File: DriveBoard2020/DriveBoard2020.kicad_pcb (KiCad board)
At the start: 2 copper layers, 124.5 x 107.4 mm, 69 parts, among them SW0 SW_SPST, SW1 SW_Push, SW3 SW_Push, SW5 SW_Push, SW7 SW_Push, SW8 SW_Push, SW9 SW_Push, U1 MAX_3232, U2 MAX_3232, U3 OKI, U4 TM4C129E_Launchpad, U5 MAX_3232, U6 OKI, U7 OKI, U8 LDD-1500L

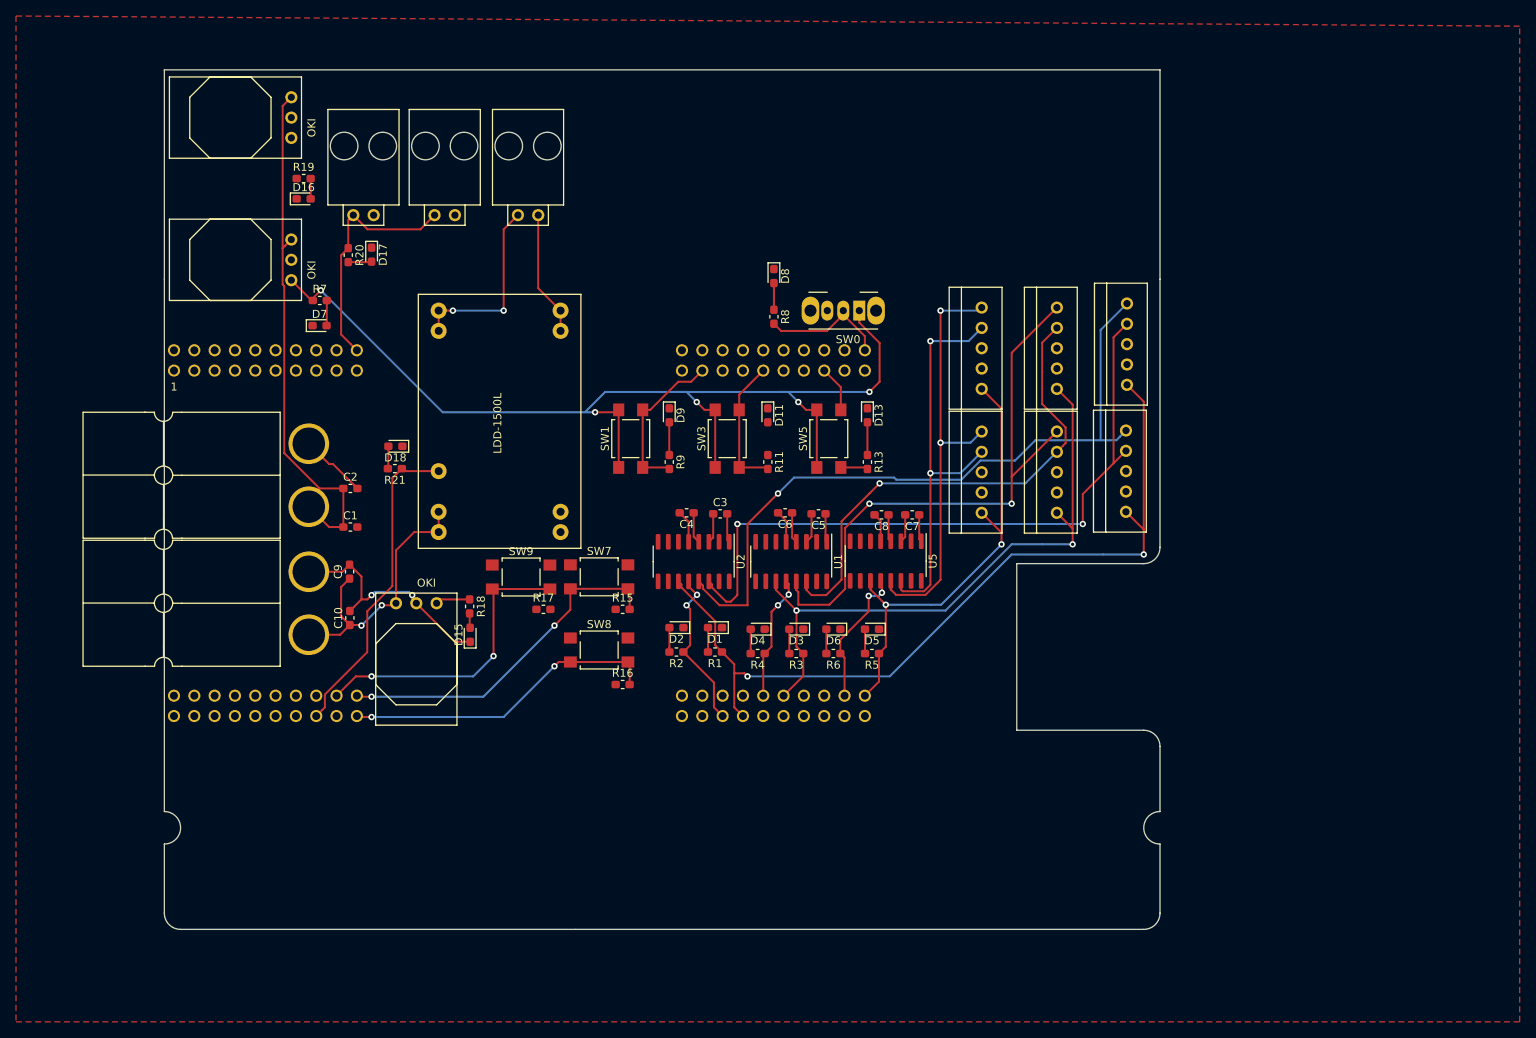
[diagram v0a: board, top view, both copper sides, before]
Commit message: cleaned up layout and generated gerbs
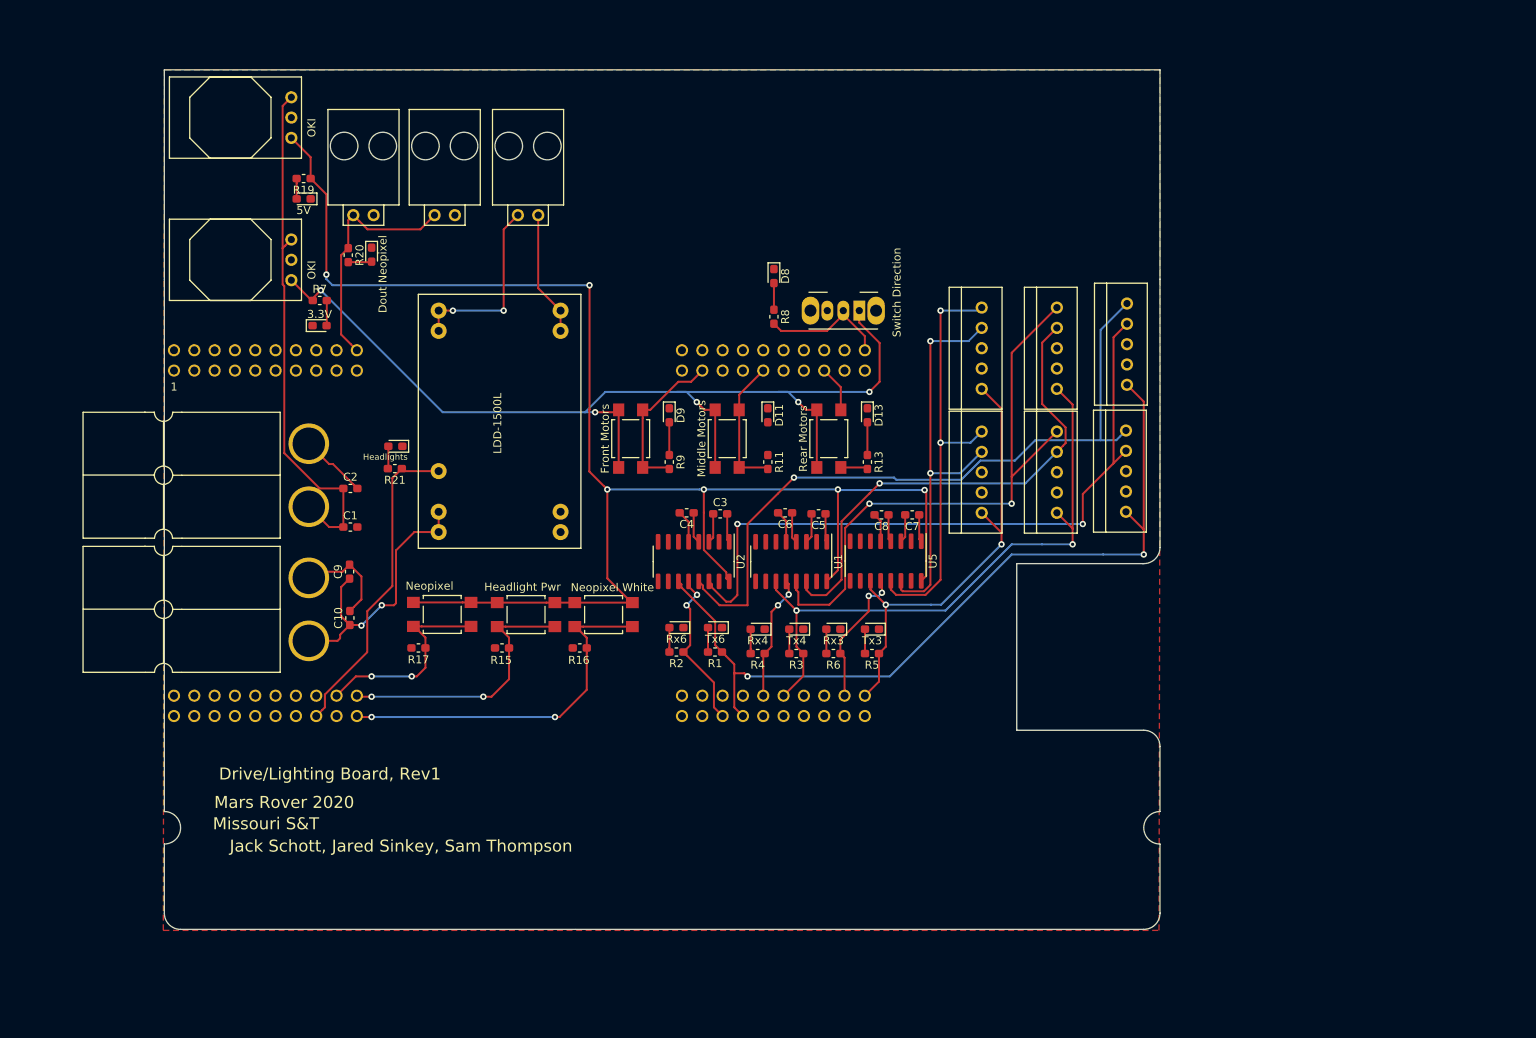
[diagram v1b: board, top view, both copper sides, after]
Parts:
- removed D15: G_LED, LED_SMD:LED_0603_1608Metric_Pad1.05x0.95mm_HandSolder
- removed R18: 500, Resistor_SMD:R_0603_1608Metric_Pad1.05x0.95mm_HandSolder
- removed U7: OKI, MRDT_Devices:OKI_Horizontal
- Dout Neopixel: renamed from D17
- Front Motors: renamed from SW1
- Headlight Pwr: renamed from SW7
- Middle Motors: renamed from SW3
- Neopixel White: renamed from SW8
- Rear Motors: renamed from SW5
- Switch Direction: renamed from SW0
- moved R17 16.3 mm to (104.9, 100.6)
- moved R15 15.8 mm to (115.4, 100.6)
- moved Neopixel 10.9 mm to (107.9, 96.4)
- moved Headlight Pwr 10.3 mm to (118.4, 96.4)
- moved R16 7.05 mm to (125.1, 100.6)
- moved Neopixel White 4.46 mm to (128.1, 96.4)
- moved Conn8 0.76 mm to (87.6, 103.6)
- turned 5V to 180 degrees
- turned R19 to 180 degrees
- renumbered D7 to 3.3V, D16 to 5V, D18 to Headlights, SW9 to Neopixel, D6 to Rx3, D4 to Rx4, D2 to Rx6, D5 to Tx3, D3 to Tx4, D1 to Tx6
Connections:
- Headlight Pwr pad 1: +5VL -> +5V
- Neopixel pad 1: +5VL -> +5V
- Neopixel White pad 1: +5VL -> +5V
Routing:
- net +5V: track 0.00 -> 198.4 mm, vias 0 -> 6
- net GNDA: track 29.3 -> 12.5 mm, vias 2 -> 0
- net NeoPixel_Pattern: track 37.3 -> 25.6 mm
- net Headlight_Power: track 43.7 -> 34.4 mm
- net NeoPixel_White: track 39.7 -> 46.0 mm
- net +5VA: track 4.33 -> 0.00 mm
- net Net-(D15-Pad2): track 1.82 -> 0.00 mm
- net +12VA: track 34.7 -> 35.3 mm
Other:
- board text added: "Drive/Lighting Board, Rev1"
- board text added: "Jack Schott, Jared Sinkey, Sam Thompson"
- board text added: "Mars Rover 2020"
- board text added: "Missouri S&T"

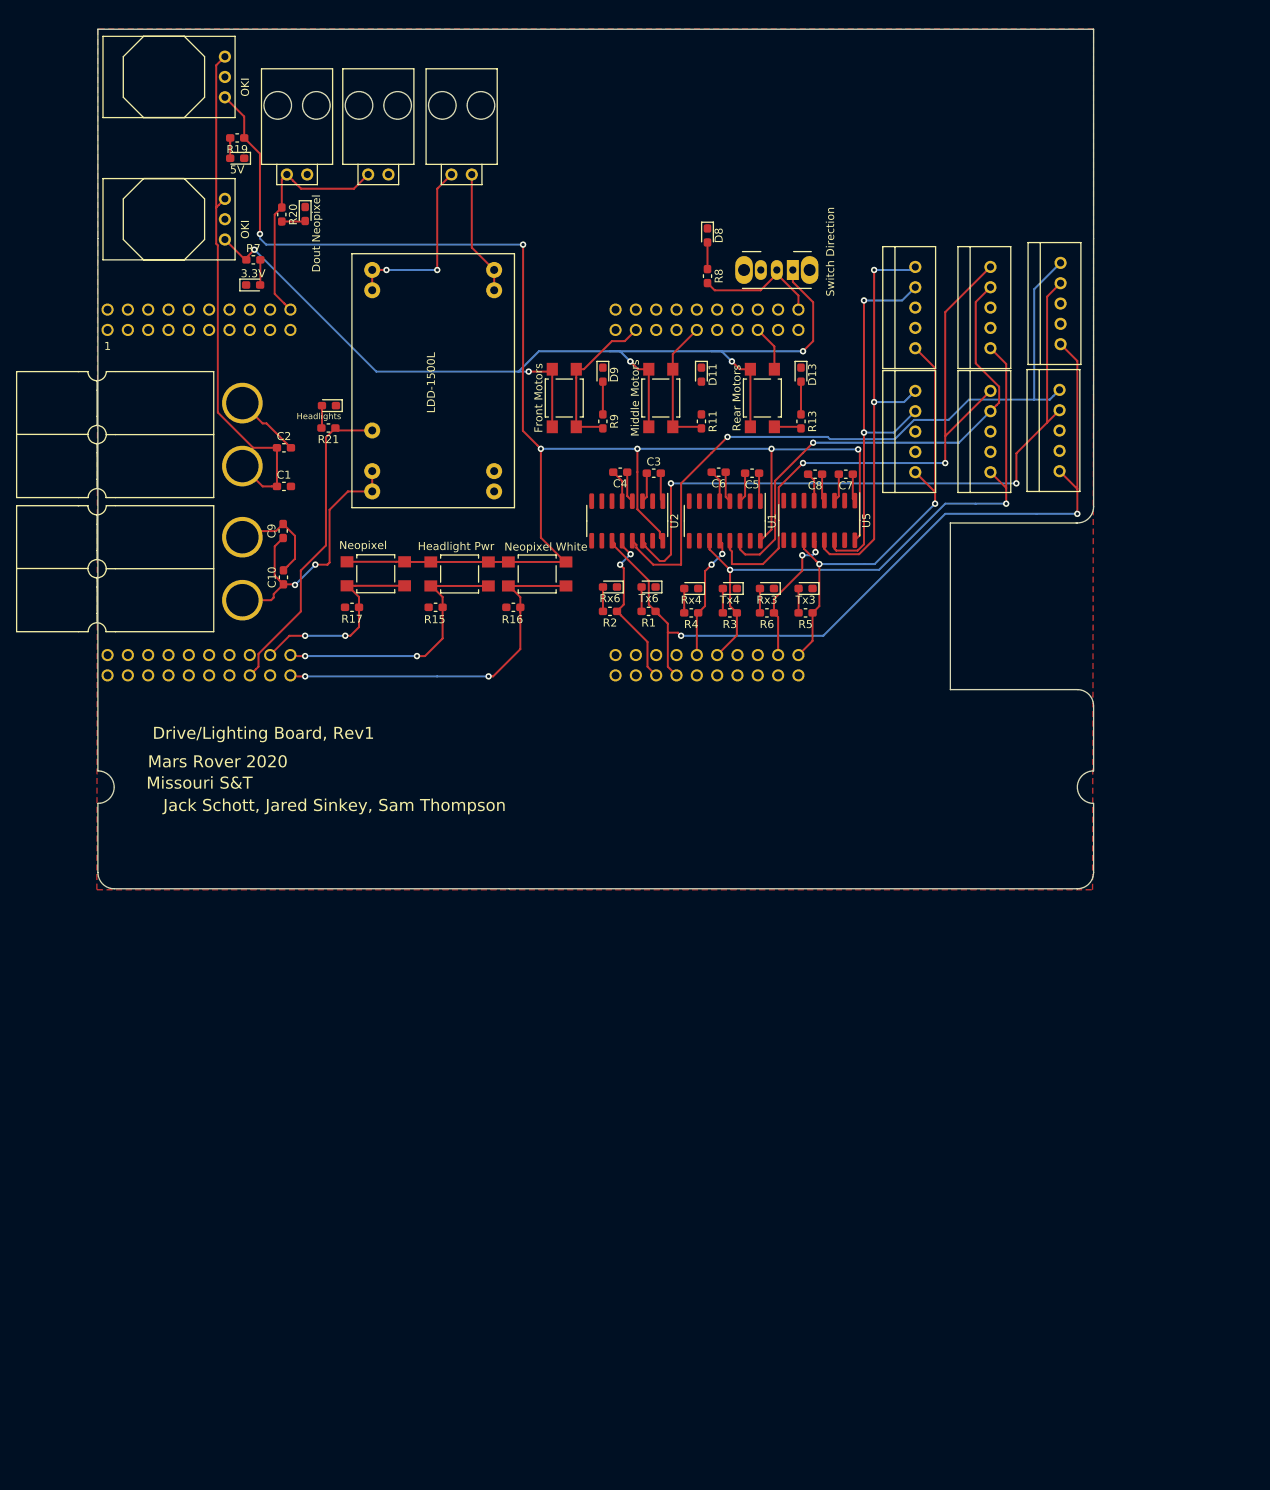
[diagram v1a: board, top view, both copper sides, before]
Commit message: imported netlist to layout
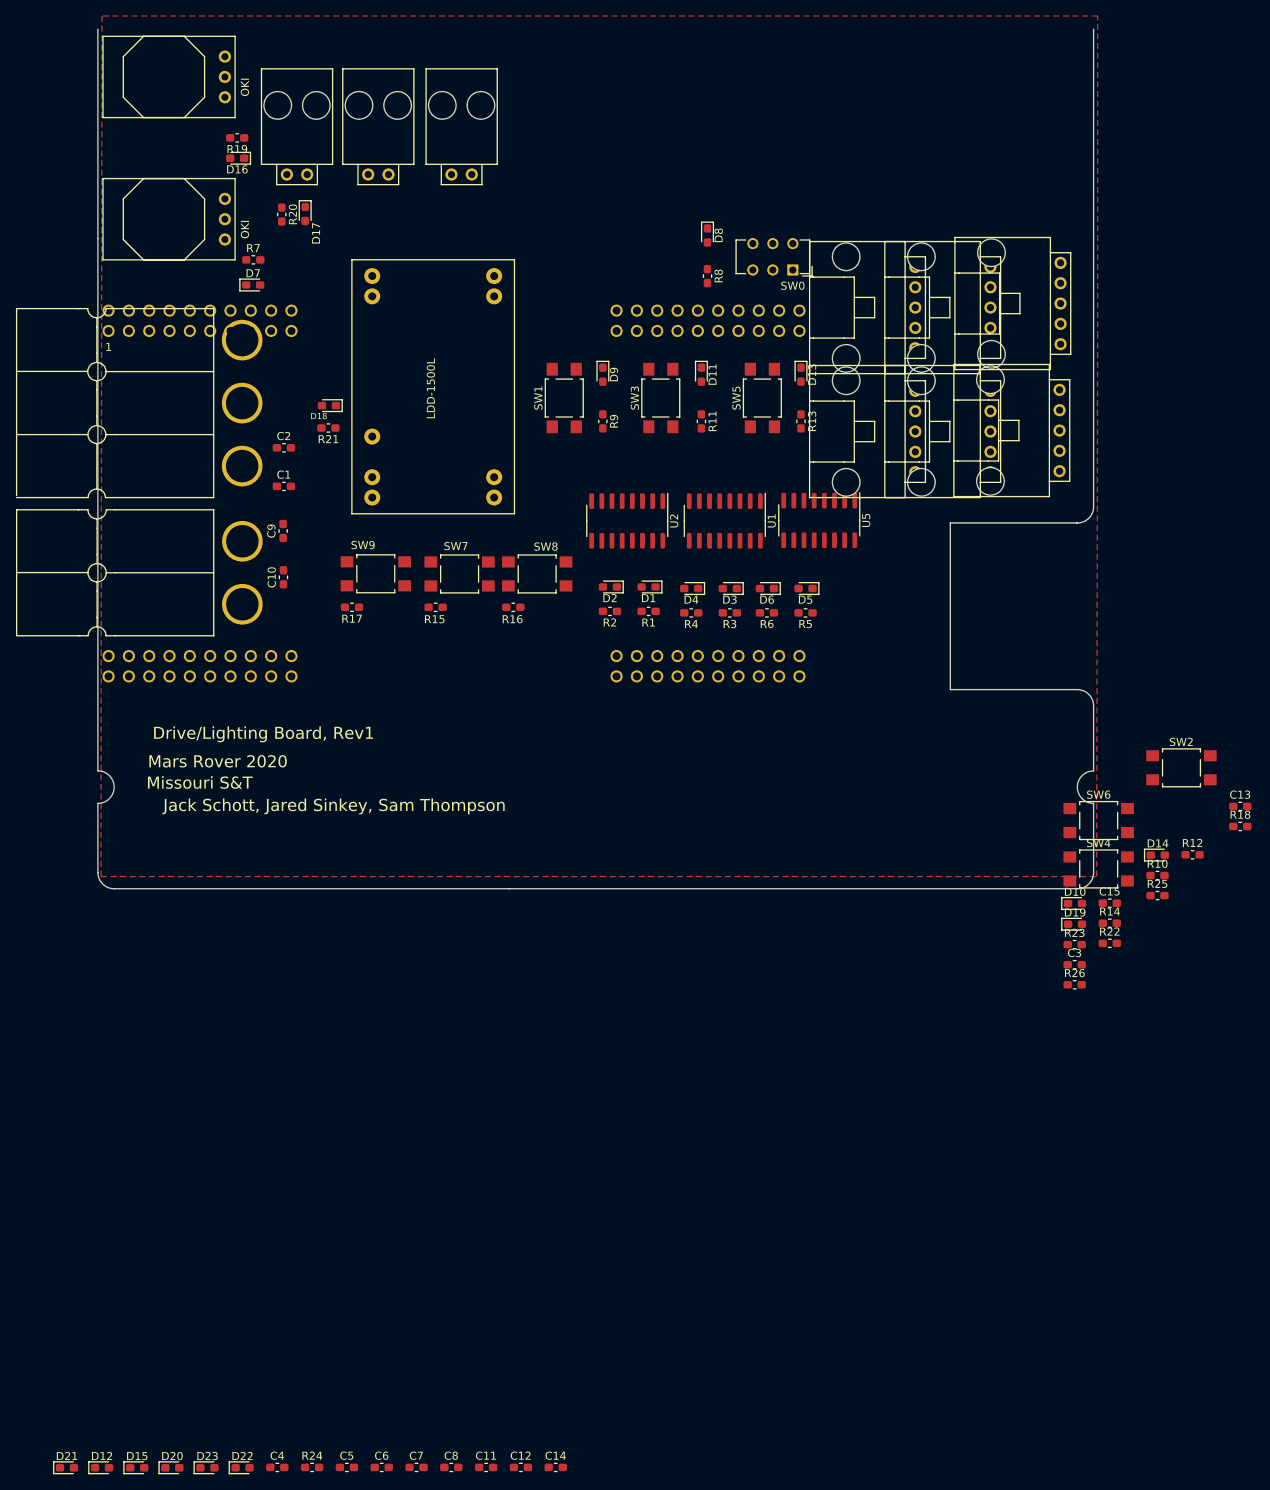
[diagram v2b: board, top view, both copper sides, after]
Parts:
- removed Switch Direction: SW_SPST, Button_Switch_THT:SW_CuK_OS102011MA1QN1_SPDT_Angled
- added C11: .1uF, Capacitor_SMD:C_0603_1608Metric_Pad1.05x0.95mm_HandSolder, F.Cu at (121.7, 208.1)
- added C12: .1uF, Capacitor_SMD:C_0603_1608Metric_Pad1.05x0.95mm_HandSolder, F.Cu at (126.0, 208.1)
- added C13: .1uF, Capacitor_SMD:C_0603_1608Metric_Pad1.05x0.95mm_HandSolder, F.Cu at (215.9, 125.5)
- added C14: 10uF, Capacitor_SMD:C_0603_1608Metric_Pad1.05x0.95mm_HandSolder, F.Cu at (130.4, 208.1)
- added C15: 10uF, Capacitor_SMD:C_0603_1608Metric_Pad1.05x0.95mm_HandSolder, F.Cu at (199.6, 137.6)
- added D10: LED, LED_SMD:LED_0603_1608Metric_Pad1.05x0.95mm_HandSolder, F.Cu at (195.3, 137.6)
- added D12: LED, LED_SMD:LED_0603_1608Metric_Pad1.05x0.95mm_HandSolder, F.Cu at (73.7, 208.1)
- added D14: LED, LED_SMD:LED_0603_1608Metric_Pad1.05x0.95mm_HandSolder, F.Cu at (205.6, 131.6)
- added D15: LED, LED_SMD:LED_0603_1608Metric_Pad1.05x0.95mm_HandSolder, F.Cu at (78.1, 208.1)
- added D19: LED, LED_SMD:LED_0603_1608Metric_Pad1.05x0.95mm_HandSolder, F.Cu at (195.3, 140.2)
- added D20: LED, LED_SMD:LED_0603_1608Metric_Pad1.05x0.95mm_HandSolder, F.Cu at (82.5, 208.1)
- added D21: LED, LED_SMD:LED_0603_1608Metric_Pad1.05x0.95mm_HandSolder, F.Cu at (69.3, 208.1)
- added D22: LED, LED_SMD:LED_0603_1608Metric_Pad1.05x0.95mm_HandSolder, F.Cu at (91.2, 208.1)
- added D23: LED, LED_SMD:LED_0603_1608Metric_Pad1.05x0.95mm_HandSolder, F.Cu at (86.8, 208.1)
- added R10: 330, Resistor_SMD:R_0603_1608Metric_Pad1.05x0.95mm_HandSolder, F.Cu at (205.6, 134.1)
- added R12: 330, Resistor_SMD:R_0603_1608Metric_Pad1.05x0.95mm_HandSolder, F.Cu at (210.0, 131.5)
- added R14: 330, Resistor_SMD:R_0603_1608Metric_Pad1.05x0.95mm_HandSolder, F.Cu at (199.6, 140.1)
- added R18: 500, Resistor_SMD:R_0603_1608Metric_Pad1.05x0.95mm_HandSolder, F.Cu at (215.9, 128.0)
- added R22: 500, Resistor_SMD:R_0603_1608Metric_Pad1.05x0.95mm_HandSolder, F.Cu at (199.6, 142.6)
- added R23: 500, Resistor_SMD:R_0603_1608Metric_Pad1.05x0.95mm_HandSolder, F.Cu at (195.2, 142.7)
- added R24: 500, Resistor_SMD:R_0603_1608Metric_Pad1.05x0.95mm_HandSolder, F.Cu at (99.9, 208.1)
- added R25: 500, Resistor_SMD:R_0603_1608Metric_Pad1.05x0.95mm_HandSolder, F.Cu at (205.6, 136.6)
- added R26: 500, Resistor_SMD:R_0603_1608Metric_Pad1.05x0.95mm_HandSolder, F.Cu at (195.2, 147.8)
- added SW0: SW_SPST, Button_Switch_THT:SW_CuK_JS202011AQN_DPDT_Angled, F.Cu at (160.0, 58.4)
- added SW2: SW_Push, Button_Switch_SMD:SW_SPST_TL3305A, F.Cu at (208.6, 120.7)
- added SW4: SW_Push, Button_Switch_SMD:SW_SPST_TL3305A, F.Cu at (198.2, 133.3)
- added SW6: SW_Push, Button_Switch_SMD:SW_SPST_TL3305A, F.Cu at (198.2, 127.2)
- C6, C7, C8: value 1uF -> .1uF
- Conn1: footprint MRDT_Connectors:Anderson_2_Horizontal_Side_by_Side -> MRDT_Connectors:Anderson_3_Horizontal_Side_by_Side
- Conn2, Conn3, Conn4, Conn5, Conn6, Conn7: footprint MRDT_Connectors:MOLEX_SL_05_Vertical -> MRDT_Connectors:MOLEX_SL_05_Horizontal
- D17: renamed from Dout Neopixel
- R11, R13, R7, R8, R9: value 500 -> 330
- R15: value 10K -> 330
- R16, R17: value 10K -> 500
- SW1: renamed from Front Motors
- SW3: renamed from Middle Motors
- SW5: renamed from Rear Motors
- SW7: renamed from Headlight Pwr
- SW8: renamed from Neopixel White
- moved C7 135.3 mm to (113.0, 208.1), turned to 0 degrees
- moved C5 134.2 mm to (104.3, 208.1), turned to 0 degrees
- moved C8 132.2 mm to (117.3, 208.1), turned to 0 degrees
- moved C4 131.6 mm to (95.6, 208.1), turned to 0 degrees
- moved C6 131.3 mm to (108.6, 208.1), turned to 0 degrees
- moved C3 80.9 mm to (195.2, 145.3)
- moved U8 0.76 mm to (125.2, 57.1)
- moved Conn8 0.51 mm to (87.6, 104.1)
- moved U4 0.18 mm to (73.2, 110.5)
- renumbered Tx6 to D1, 5V to D16, Headlights to D18, Rx6 to D2, Tx4 to D3, Rx4 to D4, Tx3 to D5, Rx3 to D6, 3.3V to D7, Neopixel to SW9
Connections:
- net Front_Motor renamed FR_Motor
- net Middle_Motor renamed MR_Motor
- net Rear_Motor renamed RR_Motor
- C10 pad 2: GNDA -> GND
- C2 pad 1: +12V -> +3V3
- C9 pad 2: GNDA -> GND
- Conn2 pad 1: Tx6 -> Net-(Conn2-Pad1)
- Conn2 pad 4: T1_Out -> FL_Out
- Conn2 pad 5: R1_In -> FL_In
- Conn3 pad 1: Tx4 -> Net-(Conn3-Pad1)
- Conn3 pad 4: T2_Out -> ML_Out
- Conn3 pad 5: R2_In -> ML_In
- Conn4 pad 1: Tx3 -> Net-(Conn4-Pad1)
- Conn4 pad 4: T3_Out -> RL_Out
- Conn4 pad 5: R3_In -> RL_In
- Conn5 pad 1: Tx6 -> Net-(Conn5-Pad1)
- Conn5 pad 4: T1_Out -> FR_Out
- Conn5 pad 5: R1_In -> FR_In
- Conn6 pad 1: Tx4 -> Net-(Conn6-Pad1)
- Conn6 pad 4: T2_Out -> MR_Out
- Conn6 pad 5: R2_In -> MR_In
- Conn7 pad 1: Tx3 -> Net-(Conn7-Pad1)
- Conn7 pad 4: T3_Out -> RR_Out
- Conn7 pad 5: R3_In -> RR_In
- Conn8 pad 1: GNDA -> GND
- Conn8 pad 2: +12VA -> (no net)
- SW7 pad 1: +5V -> +3V3
- U1 pad 1: Net-(C5-Pad1) -> Net-(C8-Pad1)
- U1 pad 10: Net-(U1-Pad10) -> Tx4
- U1 pad 11: Tx4 -> Tx5
- U1 pad 12: Rx4 -> Rx5
- U1 pad 13: R2_In -> ML_In
- U1 pad 14: T2_Out -> ML_Out
- U1 pad 2: Net-(U1-Pad2) -> Net-(C4-Pad1)
- U1 pad 3: Net-(C5-Pad2) -> Net-(C8-Pad2)
- U1 pad 4: Net-(C6-Pad1) -> Net-(C11-Pad1)
- U1 pad 5: Net-(C6-Pad2) -> Net-(C11-Pad2)
- U1 pad 6: Net-(U1-Pad6) -> Net-(C4-Pad2)
- U1 pad 7: Net-(U1-Pad7) -> MR_Out
- U1 pad 8: Net-(U1-Pad8) -> MR_In
- U1 pad 9: Net-(U1-Pad9) -> Rx4
- U2 pad 1: Net-(C3-Pad2) -> Net-(C6-Pad1)
- U2 pad 10: Net-(U2-Pad10) -> Tx6
- U2 pad 11: Tx6 -> Tx7
- U2 pad 12: Rx6 -> Rx7
- U2 pad 13: R1_In -> FL_In
- U2 pad 14: T1_Out -> FL_Out
- U2 pad 2: Net-(U2-Pad2) -> Net-(C3-Pad1)
- U2 pad 3: Net-(C3-Pad1) -> Net-(C6-Pad2)
- U2 pad 4: Net-(C4-Pad1) -> Net-(C7-Pad1)
- U2 pad 5: Net-(C4-Pad2) -> Net-(C7-Pad2)
- U2 pad 6: Net-(U2-Pad6) -> Net-(C3-Pad2)
- U2 pad 7: Net-(U2-Pad7) -> FR_Out
- U2 pad 8: Net-(U2-Pad8) -> FR_In
- U2 pad 9: Net-(U2-Pad9) -> Rx6
- U4 pad PA6: Net-(U4-PadPA6) -> Rx2
- U4 pad PA7: Net-(U4-PadPA7) -> Tx2
- U4 pad PC4: Net-(U4-PadPC4) -> Rx7
- U4 pad PC5: Net-(U4-PadPC5) -> Tx7
- U4 pad PC6: Net-(U4-PadPC6) -> Rx5
- U4 pad PC7: Headlight_OnOff_PWM -> Tx5
- U5 pad 1: Net-(C7-Pad1) -> Net-(C12-Pad1)
- U5 pad 10: Net-(U5-Pad10) -> Tx2
- U5 pad 13: R3_In -> RL_In
- U5 pad 14: T3_Out -> RL_Out
- U5 pad 2: Net-(U5-Pad2) -> Net-(C5-Pad1)
- U5 pad 3: Net-(C7-Pad2) -> Net-(C12-Pad2)
- U5 pad 4: Net-(C8-Pad1) -> Net-(C13-Pad1)
- U5 pad 5: Net-(C8-Pad2) -> Net-(C13-Pad2)
- U5 pad 6: Net-(U5-Pad6) -> Net-(C5-Pad2)
- U5 pad 7: Net-(U5-Pad7) -> RR_Out
- U5 pad 8: Net-(U5-Pad8) -> RR_In
- U5 pad 9: Net-(U5-Pad9) -> Rx2
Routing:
- net +5V: track 198.4 -> 0.00 mm, vias 6 -> 0
- net +3V3: track 130.6 -> 0.00 mm, vias 5 -> 0
- net Tx6: track 103.0 -> 0.00 mm, vias 2 -> 0
- net R1_In: track 88.5 -> 0.00 mm, vias 1 -> 0
- net T1_Out: track 86.7 -> 0.00 mm, vias 2 -> 0
- net Tx4: track 77.7 -> 0.00 mm, vias 2 -> 0
- net R2_In: track 74.2 -> 0.00 mm, vias 2 -> 0
- net +12V: track 66.0 -> 0.00 mm
- net T2_Out: track 62.3 -> 0.00 mm, vias 1 -> 0
- net Tx3: track 57.8 -> 0.00 mm, vias 2 -> 0
- net R3_In: track 53.0 -> 0.00 mm, vias 3 -> 0
- net T3_Out: track 50.3 -> 0.00 mm, vias 2 -> 0
- net NeoPixel_White: track 46.0 -> 0.00 mm, vias 2 -> 0
- net Headlight_OnOff_PWM: track 40.1 -> 0.00 mm
- net +12VA: track 35.3 -> 0.00 mm, vias 2 -> 0
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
